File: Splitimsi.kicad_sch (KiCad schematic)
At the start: 46 parts, among them SW1 MX_RGB, SW10 MX_RGB, SW11 MX_RGB, SW12 RotaryEncoder_Switch, SW13 MX_RGB, SW14 MX_RGB, SW15 MX_RGB, SW16 MX_RGB, SW17 MX_RGB, SW18 MX_RGB, SW19 MX_RGB, SW2 MX_RGB, SW20 MX_RGB, SW21 MX_RGB, SW22 MX_RGB, SW23 MX_RGB, SW24 MX_RGB, SW25 MX_RGB, SW26 MX_RGB, SW27 MX_RGB, SW28 MX_RGB, SW29 MX_RGB, SW3 MX_RGB, SW30 MX_RGB, SW4 MX_RGB, SW5 MX_RGB, SW6 RotaryEncoder_Switch, SW7 MX_RGB, SW8 MX_RGB, SW9 MX_RGB, U1 ProMicro, U2 TRRS

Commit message: Led DIN resistor added
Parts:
- added R1: (no value), symbol Device:R
- Dogo1: value (none) -> Conn_01x04_Male; footprint (none) -> Connector_PinSocket_2.00mm:PinSocket_1x04_P2.00mm_Vertical
- renumbered R1 to R2, R2 to R3, S2 to S1
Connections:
- net LedData: now also R1.1; no longer SW1.6 (DIN)
- new net: R1.2, SW1.6 (DIN)

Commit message: Led Power Supply connected to the MCU directly
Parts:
- R1: value (none) -> 330; footprint (none) -> Resistor_SMD:R_1206_3216Metric_Pad1.30x1.75mm_HandSolder
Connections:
- net +5V: now also SW1.3 (VDD), SW10.3 (VDD), SW11.3 (VDD), SW13.3 (VDD), SW14.3 (VDD), SW15.3 (VDD), SW16.3 (VDD), SW17.3 (VDD), SW18.3 (VDD), SW19.3 (VDD), SW2.3 (VDD), SW20.3 (VDD), SW21.3 (VDD), SW22.3 (VDD), SW23.3 (VDD), SW24.3 (VDD), SW25.3 (VDD), SW26.3 (VDD), SW27.3 (VDD), SW28.3 (VDD), SW29.3 (VDD), SW3.3 (VDD), SW30.3 (VDD), SW4.3 (VDD), SW5.3 (VDD), SW7.3 (VDD), SW8.3 (VDD), SW9.3 (VDD)
- net B+: no longer SW1.3 (VDD), SW10.3 (VDD), SW11.3 (VDD), SW13.3 (VDD), SW14.3 (VDD), SW15.3 (VDD), SW16.3 (VDD), SW17.3 (VDD), SW18.3 (VDD), SW19.3 (VDD), SW2.3 (VDD), SW20.3 (VDD), SW21.3 (VDD), SW22.3 (VDD), SW23.3 (VDD), SW24.3 (VDD), SW25.3 (VDD), SW26.3 (VDD), SW27.3 (VDD), SW28.3 (VDD), SW29.3 (VDD), SW3.3 (VDD), SW30.3 (VDD), SW4.3 (VDD), SW5.3 (VDD), SW7.3 (VDD), SW8.3 (VDD), SW9.3 (VDD)
- net GND: no longer Pin1.1 (Pin_1)
- new net B-: Pin1.1 (Pin_1)

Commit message: Reset button footprint changed
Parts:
- S1: value B3U-1000P -> (none); footprint digikey-footprints:Switch_Tactile_SMD_B3U-1000P -> (none)
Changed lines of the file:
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@@
       (effects (font (size 1.524 1.524)))
     )
-    (property "Value" "B3U-1000P" (id 1) (at 201.93 39.37 0)
-      (effects (font (size 1.524 1.524)))
-    )
-    (property "Footprint" "digikey-footprints:Switch_Tactile_SMD_B3U-1000P" (id 2) (at 207.01 39.37 0)
+    (property "Value" "" (id 1) (at 201.93 39.37 0)
+      (effects (font (size 1.524 1.524)) hide)
+    )
+    (property "Footprint" "" (id 2) (at 207.01 39.37 0)
       (effects (font (size 1.524 1.524)) (justify left) hide)
     )
@@
     )
     (path "/71fa3c88-abdf-4868-92dd-da7a96a3466b"
-      (reference "S1") (unit 1) (value "B3U-1000P") (footprint "digikey-footprints:Switch_Tactile_SMD_B3U-1000P")
+      (reference "S1") (unit 1) (value "B3U-1000P") (footprint "Lily58:TACT_SWITCH_TVBP06")
     )
     (path "/200aa83c-0260-4790-a345-ddeba1e13353"

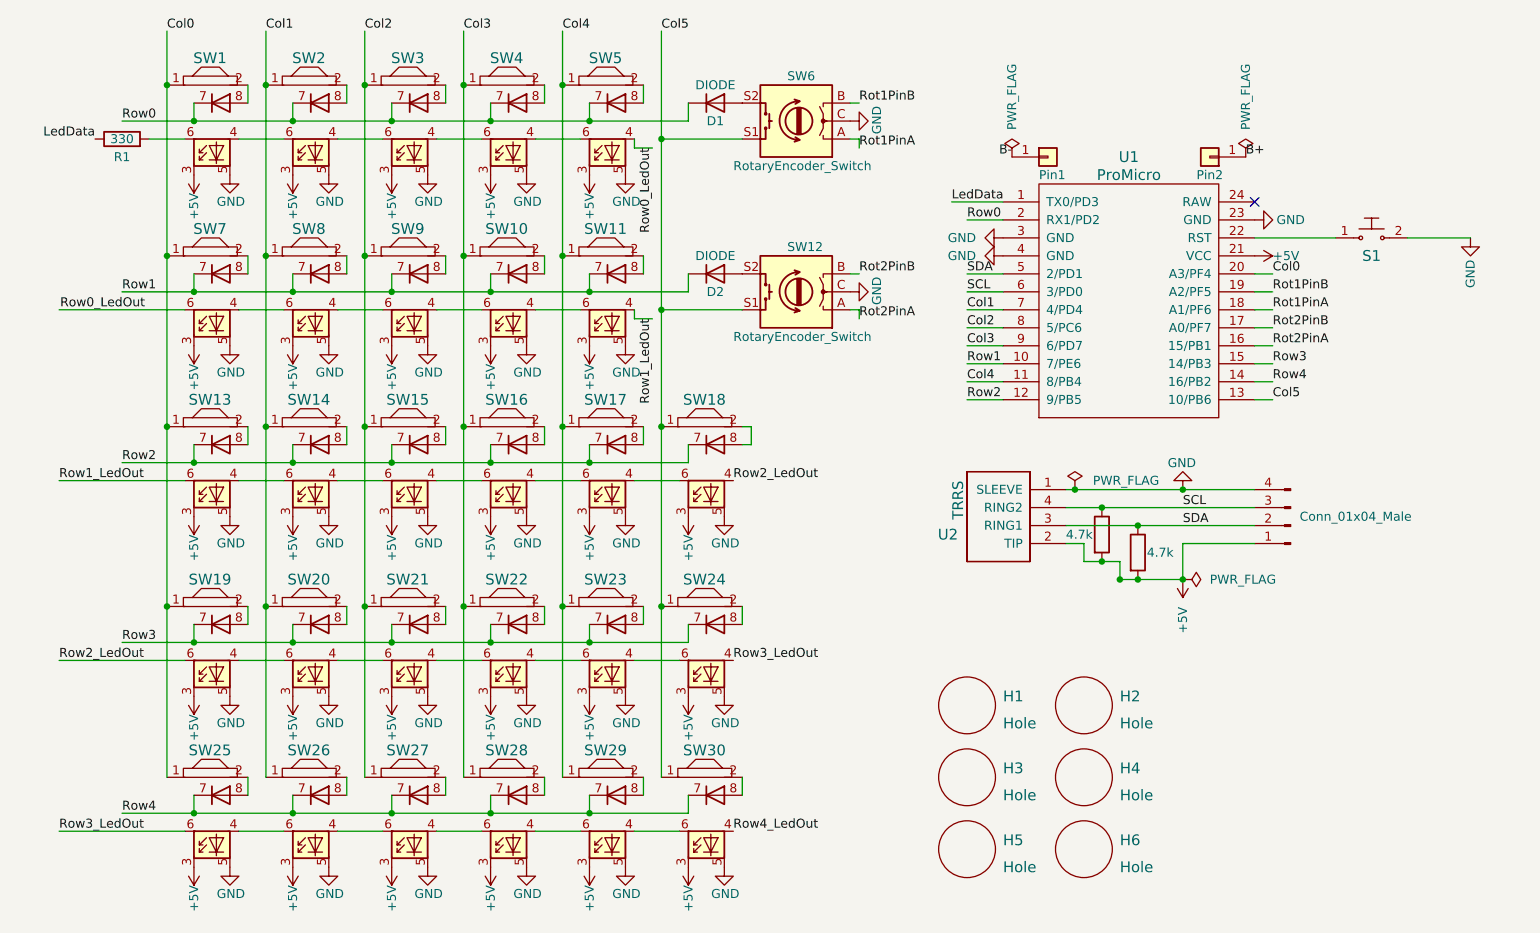
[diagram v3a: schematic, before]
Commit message: Battery on/off switch added
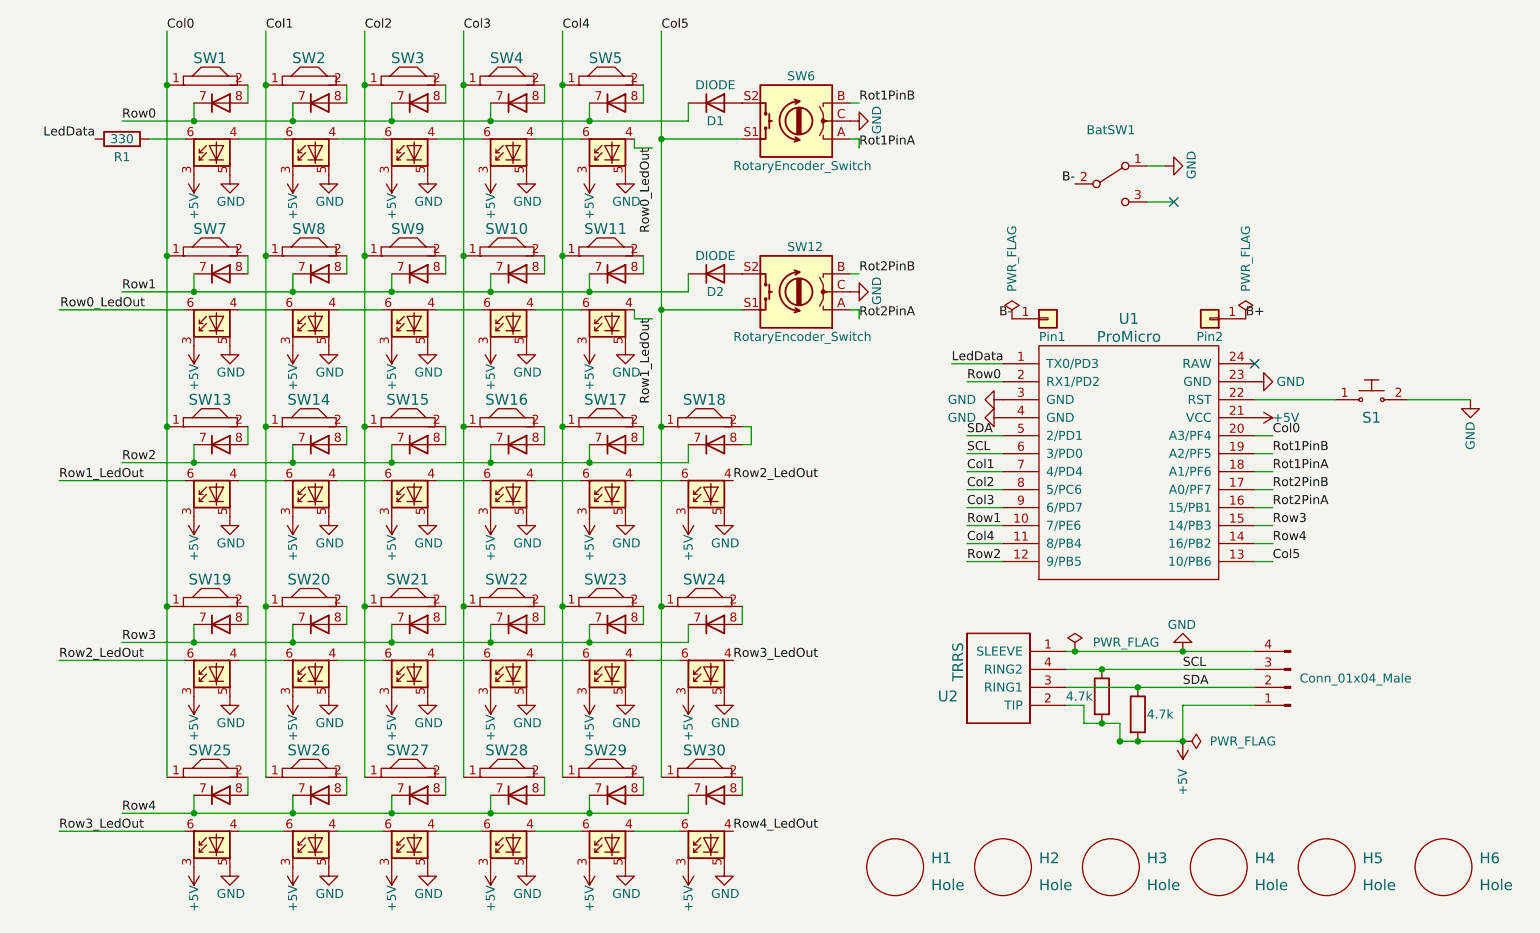
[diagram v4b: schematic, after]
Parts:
- added BatSW1: (no value), symbol Switch:SW_SPDT
- S1: value (none) -> B3U-1000P; footprint (none) -> digikey-footprints:Switch_Tactile_SMD_B3U-1000P
- SW18: value MX_RGB -> (none); footprint KeyboardCustomFPs:Kailh_HS_MX_LED_option2 -> (none)
- SW5: value MX_RGB -> (none); footprint KeyboardCustomFPs:Kailh_HS_MX_LED -> (none)
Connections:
- net B-: now also BatSW1.2 (B)
- net GND: now also BatSW1.1 (A)
- no-connect marks 1 -> 2
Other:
- moved on the sheet: H1, H2, H3, H4, H5, H6, Pin1, Pin2, S1, U1, U2

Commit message: Battery SW 3D view added
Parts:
- SW18: value (none) -> MX_RGB; footprint (none) -> KeyboardCustomFPs:Kailh_HS_MX_LED_option2
- SW5: value (none) -> MX_RGB; footprint (none) -> KeyboardCustomFPs:Kailh_HS_MX_LED_option3
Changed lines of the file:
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@@
       (effects (font (size 1.524 1.524)))
     )
-    (property "Value" "" (id 1) (at 107.7276 67.3151 0)
-      (effects (font (size 1.524 1.524)) hide)
-    )
-    (property "Footprint" "" (id 2) (at 106.5571 64.655 0)
+    (property "Value" "MX_RGB" (id 1) (at 107.7276 67.3151 0)
+      (effects (font (size 1.524 1.524)) hide)
+    )
+    (property "Footprint" "KeyboardCustomFPs:Kailh_HS_MX_LED_option2" (id 2) (at 106.5571 64.655 0)
       (effects (font (size 1.524 1.524)) hide)
     )
@@
       (effects (font (size 1.524 1.524)))
     )
-    (property "Value" "" (id 1) (at 93.7576 19.0551 0)
-      (effects (font (size 1.524 1.524)) hide)
-    )
-    (property "Footprint" "" (id 2) (at 92.5871 16.395 0)
+    (property "Value" "MX_RGB" (id 1) (at 93.7576 19.0551 0)
+      (effects (font (size 1.524 1.524)) hide)
+    )
+    (property "Footprint" "KeyboardCustomFPs:Kailh_HS_MX_LED_option3" (id 2) (at 92.5871 16.395 0)
       (effects (font (size 1.524 1.524)) hide)
     )
@@
     )
     (path "/b45cddbf-b7e0-4bd2-b955-fc7bd108333a"
-      (reference "BatSW1") (unit 1) (value "SW_SPDT") (footprint "davidphilip:SPDT_C128955")
+      (reference "BatSW1") (unit 1) (value "SW_SPDT") (footprint "batterysw:MSK12C02")
     )
     (path "/cefa7dfe-2569-4624-baca-5c5512c57761"

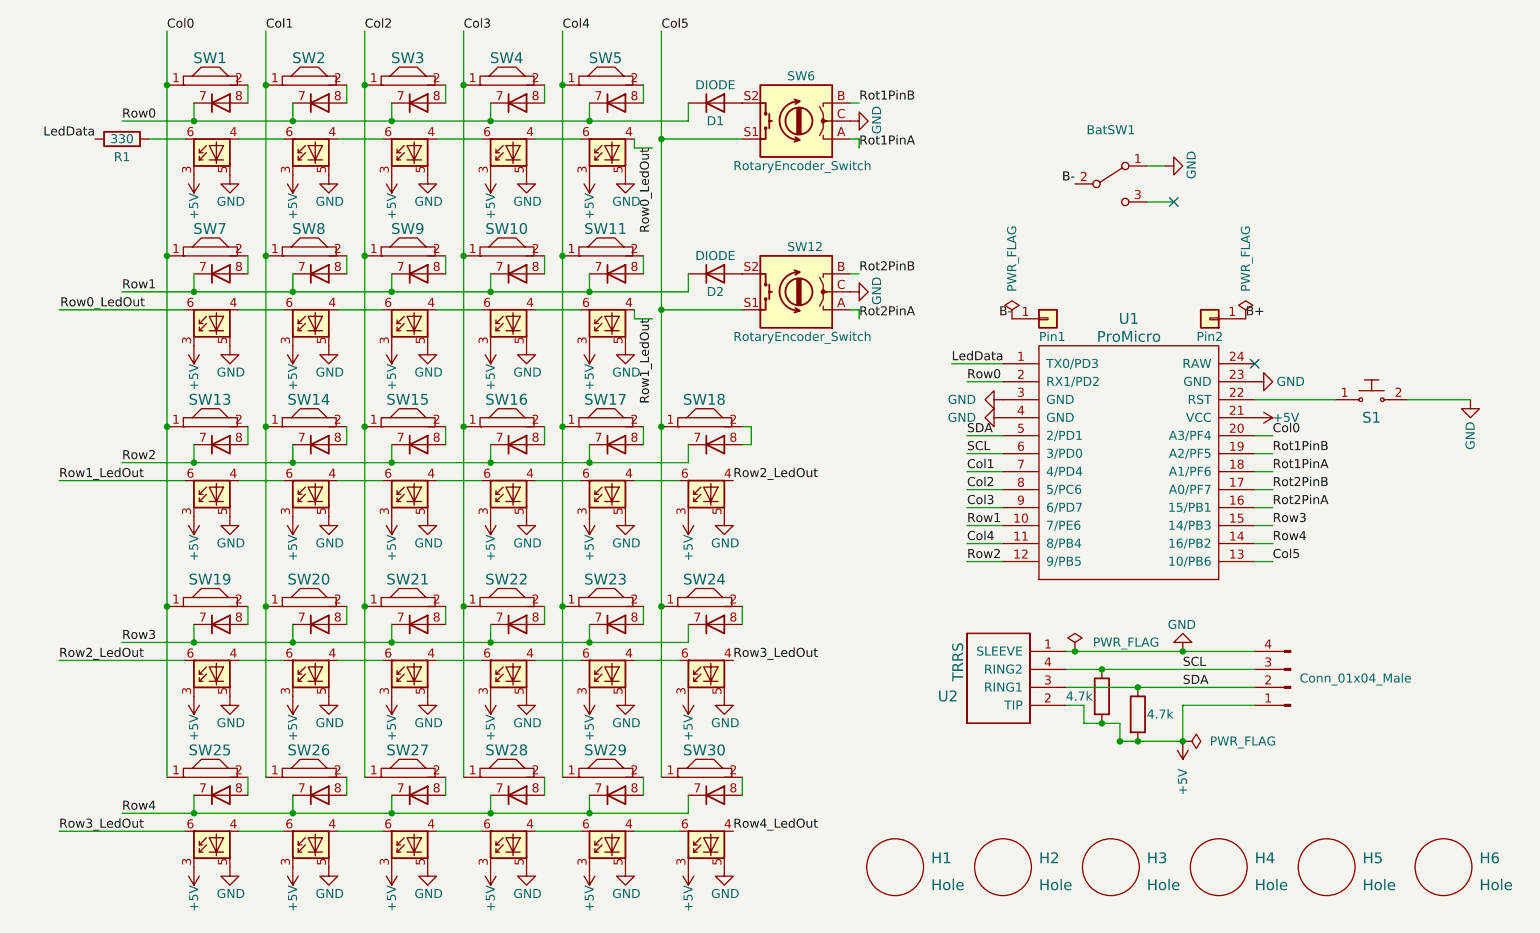
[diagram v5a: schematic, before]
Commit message: _L added to indicate the left board  to all track tags
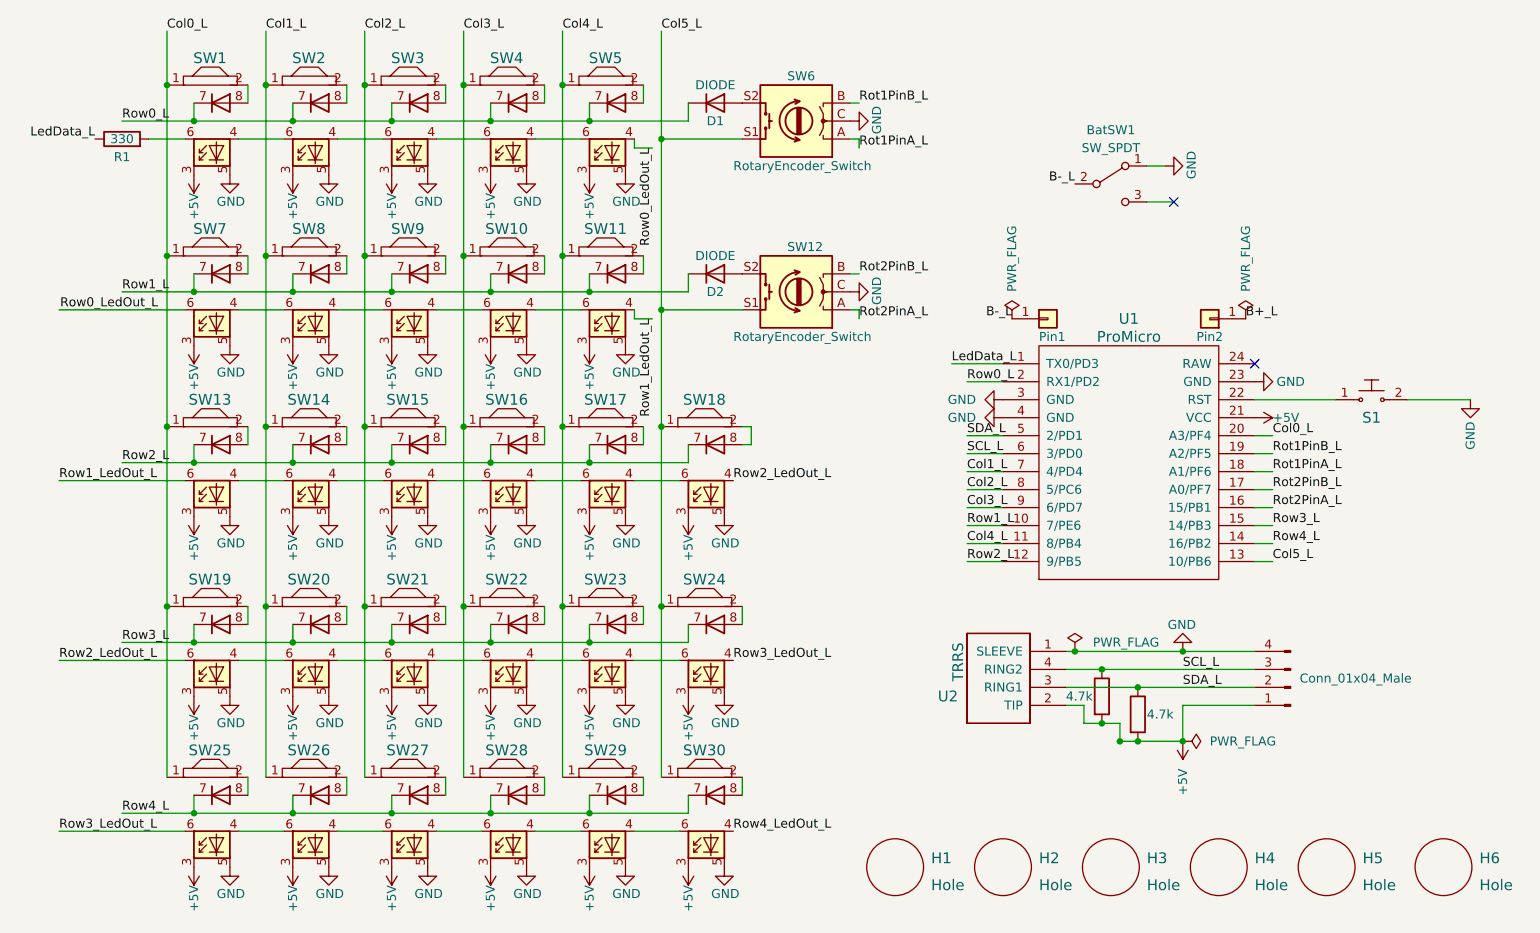
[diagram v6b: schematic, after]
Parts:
- BatSW1: value (none) -> SW_SPDT; footprint (none) -> batterysw:MSK12C02
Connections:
- net B+ renamed B+_L
- net B- renamed B-_L
- net Col0 renamed Col0_L
- net Col1 renamed Col1_L
- net Col2 renamed Col2_L
- net Col3 renamed Col3_L
- net Col4 renamed Col4_L
- net Col5 renamed Col5_L
- net LedData renamed LedData_L
- net Rot1PinA renamed Rot1PinA_L
- net Rot1PinB renamed Rot1PinB_L
- net Rot2PinA renamed Rot2PinA_L
- net Rot2PinB renamed Rot2PinB_L
- net Row0 renamed Row0_L
- net Row0_LedOut renamed Row0_LedOut_L
- net Row1 renamed Row1_L
- net Row1_LedOut renamed Row1_LedOut_L
- net Row2 renamed Row2_L
- net Row2_LedOut renamed Row2_LedOut_L
- net Row3 renamed Row3_L
- net Row3_LedOut renamed Row3_LedOut_L
- net Row4 renamed Row4_L
- net Row4_LedOut renamed Row4_LedOut_L
- net SCL renamed SCL_L
- net SDA renamed SDA_L

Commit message: trrs jack adjustments
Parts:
- SW18: value MX_RGB -> (none); footprint KeyboardCustomFPs:Kailh_HS_MX_LED_option2 -> (none)
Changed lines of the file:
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@@
       (effects (font (size 1.524 1.524)))
     )
-    (property "Value" "MX_RGB" (id 1) (at 107.7276 67.3151 0)
-      (effects (font (size 1.524 1.524)) hide)
-    )
-    (property "Footprint" "KeyboardCustomFPs:Kailh_HS_MX_LED_option2" (id 2) (at 106.5571 64.655 0)
+    (property "Value" "" (id 1) (at 107.7276 67.3151 0)
+      (effects (font (size 1.524 1.524)) hide)
+    )
+    (property "Footprint" "" (id 2) (at 106.5571 64.655 0)
       (effects (font (size 1.524 1.524)) hide)
     )
@@
     )
     (path "/26d58434-7bc0-4330-aacc-ebafc1af4dff"
-      (reference "SW18") (unit 1) (value "MX_RGB") (footprint "KeyboardCustomFPs:Kailh_HS_MX_LED_option2")
+      (reference "SW18") (unit 1) (value "MX_RGB") (footprint "KeyboardCustomFPs:Kailh_HS_MX_LED_option4")
     )
     (path "/0cb1d01e-f5f0-4c79-8ca3-b02247355dc9"

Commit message: Trrs position tests
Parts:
- SW18: value (none) -> MX_RGB; footprint (none) -> KeyboardCustomFPs:Kailh_HS_MX_LED_option4
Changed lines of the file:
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@@
       (effects (font (size 1.524 1.524)))
     )
-    (property "Value" "" (id 1) (at 107.7276 67.3151 0)
+    (property "Value" "MX_RGB" (id 1) (at 107.7276 67.3151 0)
       (effects (font (size 1.524 1.524)) hide)
     )
-    (property "Footprint" "" (id 2) (at 106.5571 64.655 0)
+    (property "Footprint" "KeyboardCustomFPs:Kailh_HS_MX_LED_option4" (id 2) (at 106.5571 64.655 0)
       (effects (font (size 1.524 1.524)) hide)
     )
